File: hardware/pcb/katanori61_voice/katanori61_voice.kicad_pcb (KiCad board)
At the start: 4 copper layers, 82 x 37.4 mm, 218 parts, among them J10 BAT (JST-PH), J13 USB-C, J15 MIC RISER, J2 OLED, J5 SPK OUT, J6 BTN2, J7 REED+TOGGLE, Q1 MMUN2133LT1G, Q103 LBSS138WT1G, Q104 S9013W, U1 TPS61090RSAR, U102 XU316-1024-QF60B-C32, U103 W25Q32JVSSIQ, U106 SN74LVC125APWR, U108 TLV320AIC3204IRHBR, U109 TPA6211A1DGNR, U110 TPS62827DMQR, U111 ME6211C18M5G-N, U112 TPS62065DSGR, U118 SGM2036S-3.3XXDH4G/TR, U2 MCP73871-2CCI/ML, U3 INA226AIDGSR, U4 AS5600-ASOM, U5 ESP32-S3-WROOM-1U-N16R8, X101 24MHz 12pF

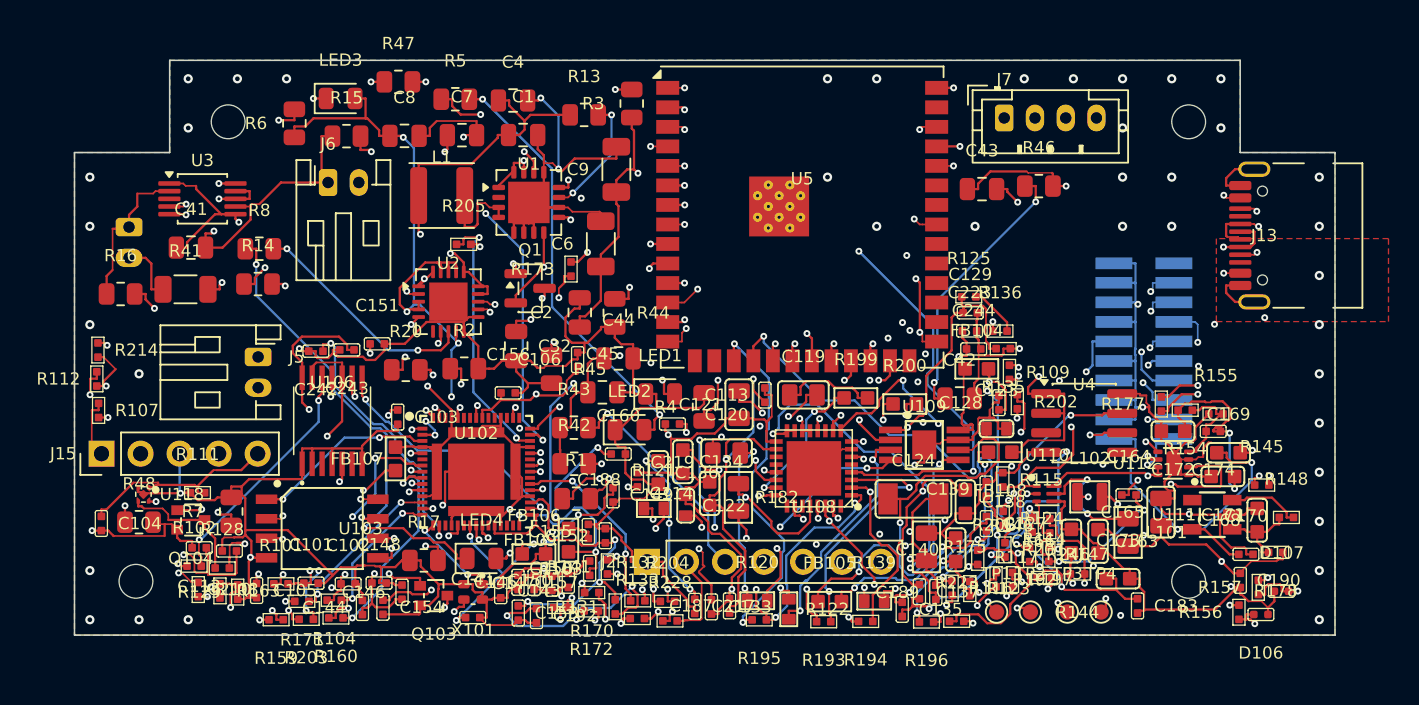
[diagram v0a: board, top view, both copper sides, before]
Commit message: 統合基板: JTAG をテストパッドに・多角形パッド・自動配線 5 回目（15 パス・ネックダウン無し）
- J105（20 ピン）を外し、XU316 のそばに 2×4 のテストパッド J16 を置く
- DSN: 回ったパッド・多角形のパッドを凸包の多角形で渡す（U118 の間隔違反が消えた）
- route.py: 板ごとに Freerouting の設定を明示（CLI の設定が全体の設定ファイルに残るため）
- 結果: 未配線 6 ネット（U102 の水晶・PLL・I2S の周りだけ）、R46/ESP_EN の間隔 0.1147 が 3 件
- gen_sch_voice / gen_pcb_voice には次の段（受動部品を 0402/0603 に・線 0.2 すきま 0.15）の
  コードも入っているが、この出力はその前の規則で作った物
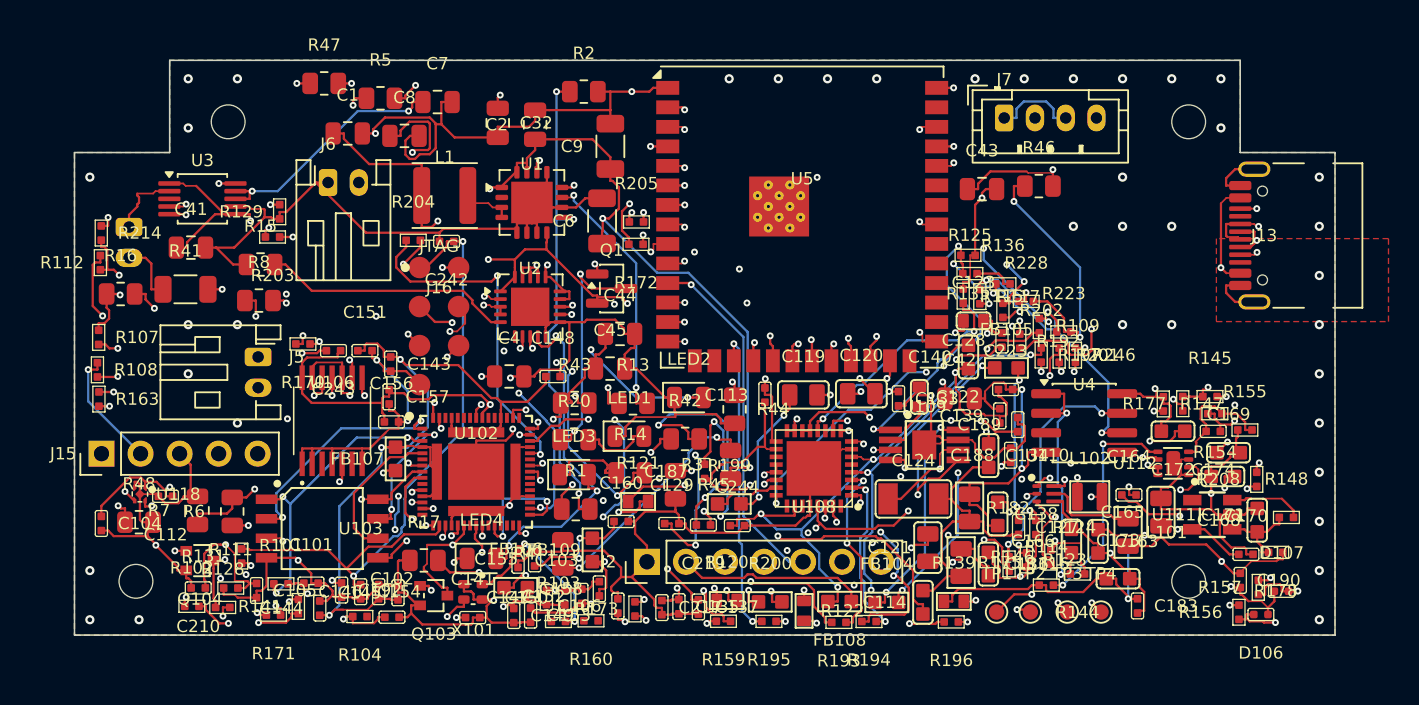
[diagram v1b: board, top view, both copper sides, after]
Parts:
- removed the C104 at (41.7, 70.1)
- removed the C129 at (98.3, 56.4)
- removed the C164 at (108.6, 68.3)
- removed the C168 at (117.0, 69.9)
- removed the C174 at (114.1, 64.1)
- removed the FB108 at (100.2, 65.5)
- removed J105: ~, voicepe:JTAG_2X10_1.27_SMD
- removed the R107 at (41.6, 62.8)
- removed the R120 at (84.4, 75.2)
- removed the R147 at (103.4, 72.1)
- removed the R175 at (95.4, 71.7)
- removed the R228 at (78.8, 76.5)
- removed the U108 at (88.1, 66.6)
- removed the U111 at (114.0, 69.6)
- removed the U112 at (111.5, 66.2)
- added FB104: 600R, voicepe:L0603, F.Cu at (92.9, 75.3)
- added R112: 3.3K, voicepe:R0402, F.Cu at (41.7, 53.2)
- added R114: 0R, voicepe:R0402, F.Cu at (103.2, 74.2)
- added R115: 10K, voicepe:R0402, F.Cu at (97.8, 55.3)
- added R116: 0R, voicepe:R0402, F.Cu at (100.8, 72.8)
- added R125: 4.7K, voicepe:R0402, F.Cu at (98.3, 53.9)
- added R144: 22R, voicepe:R0402, F.Cu at (105.3, 73.4)
- added R146: 100K, voicepe:R0402, F.Cu at (103.5, 72.3)
- added R154: 51K, voicepe:R0402, F.Cu at (114.2, 63.0)
- added R156: 22R, voicepe:R0402, F.Cu at (115.8, 75.9)
- added R157: 22R, voicepe:R0402, F.Cu at (117.0, 74.3)
- added R178: 0R, voicepe:R0402, F.Cu at (118.2, 72.0)
- added R208: 100K, voicepe:R0402, F.Cu at (116.9, 67.3)
- C104: renamed from R108; value 100R -> 100nF; footprint voicepe:R0402 -> voicepe:C0402
- C129: renamed from R125; value 4.7K -> 10nF; footprint voicepe:R0402 -> voicepe:C0402
- C164: renamed from R146; value 100K -> 120pF; footprint voicepe:R0402 -> voicepe:C0402
- C168: renamed from R178; value 0R -> 2.2uF; footprint voicepe:R0402 -> voicepe:C0603
- C174: renamed from R154; value 51K -> 22pF; footprint voicepe:R0402 -> voicepe:C0402
- FB108: renamed from R123; value 10K -> 120R; footprint voicepe:R0402 -> voicepe:L0603
- J16: renamed from R223; value 4.7K -> XU316 JTAG; footprint voicepe:R0402 -> katanori:JTAG_TP_2x4_P2.54mm
- R102: renamed from R204; value 0R -> 100R
- R107: renamed from R102; value 100R -> 47K
- R108: renamed from R205; value 0R -> 100R
- R117: renamed from R115; value 10K -> 0R
- R120: renamed from FB104; value 600R -> 15K; footprint voicepe:L0603 -> voicepe:R0603
- R123: renamed from R116; value 0R -> 10K
- R124: renamed from R117; value 0R -> 10K
- R141: renamed from R133; value 22R -> 0R
- R147: renamed from R144; value 22R -> 22.1K
- R159: renamed from R132; value 22R -> 100K
- R160: renamed from R159; value 100K -> 0R
- R175: renamed from R124; value 10K -> 0R; footprint voicepe:R0402 -> voicepe:R0805
- R192: renamed from R156; value 22R -> 0R
- R193: renamed from R157; value 22R -> 0R
- R223: renamed from R109; value 0R -> 4.7K
- R228: renamed from R246; value 0R -> 4.7K
- U108: renamed from R112; value 3.3K -> TLV320AIC3204IRHBR; footprint voicepe:R0402 -> voicepe:TLV320AIC3204IRHBR
- U111: renamed from R114; value 0R -> ME6211C18M5G-N; footprint voicepe:R0402 -> voicepe:SOT-23-5
- U112: renamed from R208; value 100K -> TPS62065DSGR; footprint voicepe:R0402 -> voicepe:DFN8G-0.5-2X2MM
- moved U108 47.0 mm to (88.1, 66.6), turned to 180 degrees
- moved J16 38.8 mm to (63.7, 57.3)
- moved R205 33.6 mm to (76.6, 50.5), turned to 0 degrees
- moved R203 32.0 mm to (52.9, 51.5)
- moved R102 31.0 mm to (47.6, 75.5)
- moved LED3 28.8 mm to (72.5, 67.0)
- moved R193 27.4 mm to (89.7, 76.6), turned to 180 degrees
- moved R14 27.2 mm to (76.2, 66.8)
- moved R6 25.6 mm to (50.3, 69.4)
- moved R108 25.2 mm to (41.5, 60.1), turned to 270 degrees
- moved R197 25.2 mm to (102.9, 59.2), turned to 270 degrees
- moved R129 24.9 mm to (53.3, 49.9)
- moved R170 24.6 mm to (54.9, 58.5), turned to 180 degrees
- moved R131 24.5 mm to (50.9, 72.3)
- moved R3 24.4 mm to (82.7, 66.3)
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- renumbered R201 to R109, R141 to R170, R160 to R171, R170 to R172, R171 to R173, R192 to R194, R193 to R195, R194 to R196, R195 to R197, R196 to R201, R197 to R202, R172 to R203, R173 to R204, R203 to R205, R202 to R246
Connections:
- C104 pad 1: MIC_CLK_M -> VDD_MIC
- C104 pad 2: N_U106_4Y -> GND
- C129 pad 2: N_R125_Pad2 -> GND
- C164 pad 1: N_U110_FB -> N_C164_Pad1
- C164 pad 2: N_C164_Pad1 -> N_U110_FB
- C168 pad 1: V33 -> N_U111_IN
- C168 pad 2: N_U111_IN -> GND
- C174 pad 1: N_U112_FB -> V09
- C174 pad 2: V09 -> N_U112_FB
- FB108 pad 1: N_U108_LDO__SELECT -> V33
- J16 pad 1: SDA -> V18
- J16 pad 2: V33 -> TMS
- R102 pad 1: N_U102_X0D35 -> N_U102_X1D22
- R102 pad 2: I2S2_BCLK -> MIC_CLK
- R107 pad 1: N_U102_X1D22 -> GND
- R107 pad 2: MIC_CLK -> MIC_DATA_M
- R108 pad 1: N_U102_X0D36 -> MIC_CLK_M
- R108 pad 2: I2S2_MCLK -> N_U106_4Y
- R109 pad 1: I2S2_LRCLK -> I2S2_MCLK
- R109 pad 2: GPIO14 -> GPIO12
- R117 pad 1: GND -> SDA
- R117 pad 2: N_U108_SPI__SELECT -> MOSI_
- R120 pad 1: N_U109_VO_ -> N_C120_Pad2
- R120 pad 2: SPKM -> N_U109_IN_
- R123 pad 1: SCL -> N_U108_LDO__SELECT
- R123 pad 2: __SS__ -> V33A
- R124 pad 1: SDA -> RST_DAC
- R124 pad 2: MOSI_ -> V33A
- R141 pad 1: N_U102_X1D19 -> XOD32
- R141 pad 2: XL_UP1 -> RST_DAC
- R147 pad 1: N_C164_Pad1 -> GND
- R147 pad 2: V33 -> N_U110_FB
- R159 pad 1: N_U102_X1D18 -> VBUS_DETEC
- R159 pad 2: XL_UP0 -> V33
- R160 pad 1: VBUS_DETEC -> N_U102_X1D00
- R160 pad 2: V33 -> I2S_DIN_SEC
- R170 pad 1: XOD32 -> N_U102_X1D01
- R170 pad 2: RST_DAC -> I2S_LRCK
- R171 pad 1: N_U102_X1D00 -> N_U102_X1D10
- R171 pad 2: I2S_DIN_SEC -> I2S_BCLK
- R172 pad 1: N_U102_X1D01 -> N_U102_X1D11
- R172 pad 2: I2S_LRCK -> I2S_MCLK
- R173 pad 1: N_U102_X1D10 -> N_U102_X1D34
- R173 pad 2: I2S_BCLK -> I2S_DIN_ESP
- R175 pad 1: RST_DAC -> GND
- R175 pad 2: V33A -> GNDA
- R192 pad 1: USB_DN -> I2S2_BCLK
- R192 pad 2: ESP_USB_DN -> GPIO13
- R193 pad 1: USB_DP -> I2S_LRCK
- R193 pad 2: ESP_USB_DP -> GPIO7
- R194 pad 1: I2S2_BCLK -> I2S_BCLK
- R194 pad 2: GPIO13 -> GPIO8
- R195 pad 1: I2S_LRCK -> I2S_MCLK
- R195 pad 2: GPIO7 -> GPIO9
- R196 pad 1: I2S_BCLK -> I2S_DIN_SEC
- R196 pad 2: GPIO8 -> GPIO10
- R197 pad 1: I2S_MCLK -> I2S_DIN_ESP
- R197 pad 2: GPIO9 -> GPIO11
- R201 pad 1: I2S_DIN_SEC -> I2S2_LRCLK
- R201 pad 2: GPIO10 -> GPIO14
- R202 pad 1: I2S_DIN_ESP -> I2S2_DATA
- R202 pad 2: GPIO11 -> GPIO15
- R203 pad 1: N_U102_X1D11 -> N_U102_X0D11
- R203 pad 2: I2S_MCLK -> I2S2_DATA
- R204 pad 1: N_U102_X1D34 -> N_U102_X0D35
- R204 pad 2: I2S_DIN_ESP -> I2S2_BCLK
- R205 pad 1: N_U102_X0D11 -> N_U102_X0D36
- R205 pad 2: I2S2_DATA -> I2S2_MCLK
- R223 pad 1: I2S2_MCLK -> SDA
- R223 pad 2: GPIO12 -> V33
- R228 pad 1: I2S_MCLK -> SCL
- R228 pad 2: I2S2_MCLK -> V33
- R246 pad 1: I2S2_DATA -> I2S_MCLK
- R246 pad 2: GPIO15 -> I2S2_MCLK
- U102 pad 33: XL_DN1 -> unconnected-(U102-X1D16-Pad33)
- U102 pad 35: XL_DN0 -> unconnected-(U102-X1D17-Pad35)
- U102 pad 36: N_U102_X1D18 -> unconnected-(U102-X1D18-Pad36)
- U102 pad 37: N_U102_X1D19 -> unconnected-(U102-X1D19-Pad37)
- U108 pad 1: MUTE_ON -> I2S_MCLK
- U108 pad 2: N_Q104_B -> I2S_BCLK
- U111 pad 1: V5 -> N_U111_IN
- U111 pad 2: N_U112_EN -> GND
- U112 pad 1: 3V3_EN -> GND
- U112 pad 2: V5 -> N_U112_SW
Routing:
- net XL_UP1: track 59.6 -> 0.00 mm, vias 3 -> 0
- net XL_DN1: track 57.3 -> 0.00 mm, vias 3 -> 0
- net XL_UP0: track 54.1 -> 0.00 mm, vias 4 -> 0
- net XL_DN0: track 50.4 -> 0.00 mm, vias 2 -> 0
- net I2S_DIN_SEC: track 64.5 -> 16.6 mm
- net VDDIO: track 123.0 -> 76.9 mm, vias 12 -> 7
- net RST_N: track 72.0 -> 37.0 mm, vias 5 -> 4
- net N_Q103_G: track 17.6 -> 52.1 mm, vias 2 -> 4
- net I2S2_MCLK: track 69.6 -> 35.9 mm
- net TCK: track 50.0 -> 20.6 mm
- net GND: track 597.7 -> 569.3 mm
- net V33: track 254.1 -> 227.3 mm
- net I2S_LRCK: track 33.0 -> 59.7 mm, vias 3 -> 4
- net RST_DAC: track 31.6 -> 57.6 mm
- net TMS: track 51.0 -> 26.5 mm
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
